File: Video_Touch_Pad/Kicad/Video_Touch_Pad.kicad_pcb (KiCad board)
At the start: 2 copper layers, 65 x 93 mm, 15 parts, among them J1 DE9

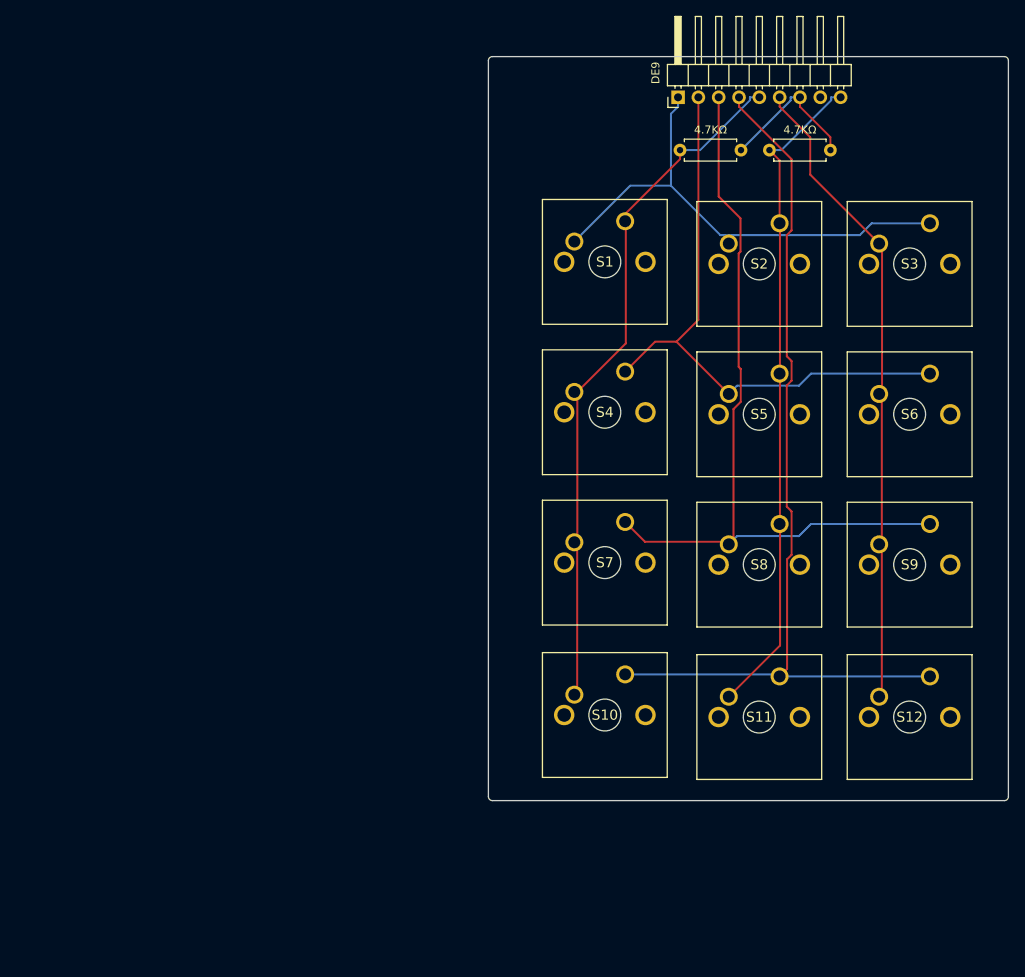
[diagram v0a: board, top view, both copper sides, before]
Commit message: Added mounting holes
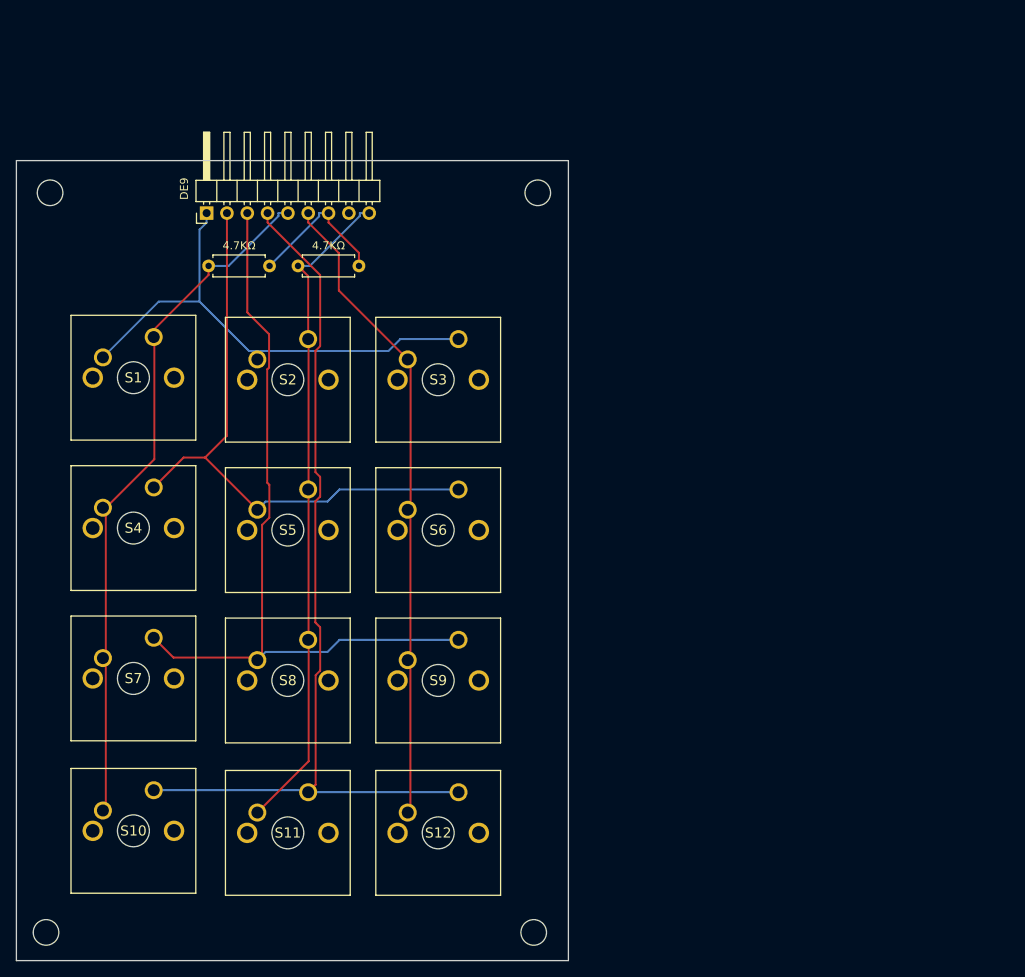
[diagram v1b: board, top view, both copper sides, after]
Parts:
- added H1: MountingHole, MountingHole:MountingHole_3.2mm_M3, F.Cu at (45.2, 49.0)
- added H2: MountingHole, MountingHole:MountingHole_3.2mm_M3, F.Cu at (106.2, 49.0)
- added H3: MountingHole, MountingHole:MountingHole_3.2mm_M3, F.Cu at (44.7, 141.5)
- added H4: MountingHole, MountingHole:MountingHole_3.2mm_M3, F.Cu at (105.7, 141.5)
- moved S11 60.7 mm to (71.1, 126.5)
- moved S12 60.7 mm to (89.9, 126.5)
- moved S7 60.7 mm to (51.8, 107.2)
- moved J1 60.7 mm to (64.8, 51.6)
- moved R2 60.7 mm to (72.6, 58.2)
- moved S1 60.7 mm to (51.8, 69.6)
- moved S10 60.7 mm to (51.8, 126.2)
- moved S2 60.7 mm to (71.1, 69.8)
- moved S3 60.7 mm to (89.9, 69.8)
- moved S4 60.7 mm to (51.8, 88.4)
- moved S5 60.7 mm to (71.1, 88.6)
- moved S6 60.7 mm to (89.9, 88.6)
- moved S8 60.7 mm to (71.1, 107.4)
- moved S9 60.7 mm to (89.9, 107.4)
- moved R1 60.7 mm to (76.2, 58.2)
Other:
- board size 65 x 93 mm -> 69 x 100 mm
